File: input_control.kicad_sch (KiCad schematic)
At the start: 17 parts, among them SW400 100SP1T1B4M2QE, SW401 100SP1T1B4M2QE, U400 CD4051BM

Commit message: pcb setup
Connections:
- no-connect marks 0 -> 16
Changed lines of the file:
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@@
 		(color 0 0 0 0)
 	)
+	(no_connect
+		(at 217.17 93.98)
+	)
+	(no_connect
+		(at 161.29 93.98)
+	)
+	(no_connect
+		(at 161.29 96.52)
+	)
+	(no_connect
+		(at 189.23 93.98)
+	)
+	(no_connect
+		(at 189.23 46.99)
+	)
+	(no_connect
+		(at 161.29 46.99)
+	)
+	(no_connect
+		(at 245.11 93.98)
+	)
+	(no_connect
+		(at 217.17 46.99)
+	)
+	(no_connect
+		(at 217.17 44.45)
+	)
+	(no_connect
+		(at 217.17 96.52)
+	)
+	(no_connect
+		(at 245.11 96.52)
+	)
+	(no_connect
+		(at 245.11 44.45)
+	)
+	(no_connect
+		(at 245.11 46.99)
+	)
+	(no_connect
+		(at 189.23 96.52)
+	)
+	(no_connect
+		(at 189.23 44.45)
+	)
+	(no_connect
+		(at 161.29 44.45)
+	)
 	(wire
 		(pts
@@
 		(dnp no)
 		(property "Reference" "VR406"
-			(at 243.84 46.736 0)
+			(at 243.84 50.292 0)
 			(effects
 				(font
@@
 		(pin "2"
 		)
+		(pin "NC1"
+		)
+		(pin "NC2"
+		)
 		(instances
 			(project "GalernaDsp"
@@
 		(dnp no)
 		(property "Reference" "VR401"
-			(at 160.02 96.266 0)
+			(at 160.02 100.076 0)
 			(effects
 				(font
@@
 		(pin "2"
 		)
+		(pin "NC1"
+		)
+		(pin "NC2"
+		)
 		(instances
 			(project "GalernaDsp"
@@
 		(dnp no)
 		(property "Reference" "VR407"
-			(at 243.84 96.266 0)
+			(at 243.84 100.076 0)
 			(effects
 				(font
@@
 		(pin "2"
 		)
+		(pin "NC1"
+		)
+		(pin "NC2"
+		)
 		(instances
 			(project "GalernaDsp"
@@
 		(dnp no)
 		(property "Reference" "VR402"
-			(at 187.96 46.736 0)
+			(at 187.96 50.292 0)
 			(effects
 				(font
@@
 		(pin "2"
 		)
+		(pin "NC1"
+		)
+		(pin "NC2"
+		)
 		(instances
 			(project "GalernaDsp"
@@
 		(dnp no)
 		(property "Reference" "VR400"
-			(at 160.02 46.736 0)
+			(at 160.02 50.292 0)
 			(effects
 				(font
@@
 		(pin "2"
 		)
+		(pin "NC2"
+		)
+		(pin "NC1"
+		)
 		(instances
 			(project ""
@@
 		(dnp no)
 		(property "Reference" "VR403"
-			(at 187.96 96.266 0)
+			(at 187.96 100.076 0)
 			(effects
 				(font
@@
 		(pin "2"
 		)
+		(pin "NC2"
+		)
+		(pin "NC1"
+		)
 		(instances
 			(project "GalernaDsp"
@@
 		(dnp no)
 		(property "Reference" "VR404"
-			(at 215.9 46.736 0)
+			(at 215.9 50.292 0)
 			(effects
 				(font
@@
 		(pin "2"
 		)
+		(pin "NC2"
+		)
+		(pin "NC1"
+		)
 		(instances
 			(project "GalernaDsp"
@@
 		(dnp no)
 		(property "Reference" "VR405"
-			(at 215.9 96.266 0)
+			(at 215.9 100.076 0)
 			(effects
 				(font
@@
 		(pin "2"
 		)
+		(pin "NC2"
+		)
+		(pin "NC1"
+		)
 		(instances

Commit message: last update
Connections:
- net POT_0_CTL: now also U400.15 (2); no longer U400.13 (0)
- net POT_1_CTL: now also U400.13 (0); no longer U400.14 (1)
- net POT_2_CTL: now also U400.14 (1); no longer U400.15 (2)
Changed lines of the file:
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@@
 		)
 	)
-	(label "POT_1_CTL"
+	(label "POT_2_CTL"
 		(at 83.82 66.04 0)
 		(effects
@@
 		)
 	)
-	(label "POT_0_CTL"
+	(label "POT_1_CTL"
 		(at 83.82 60.96 0)
 		(effects
@@
 		)
 	)
-	(label "POT_2_CTL"
+	(label "POT_0_CTL"
 		(at 83.82 71.12 0)
 		(effects

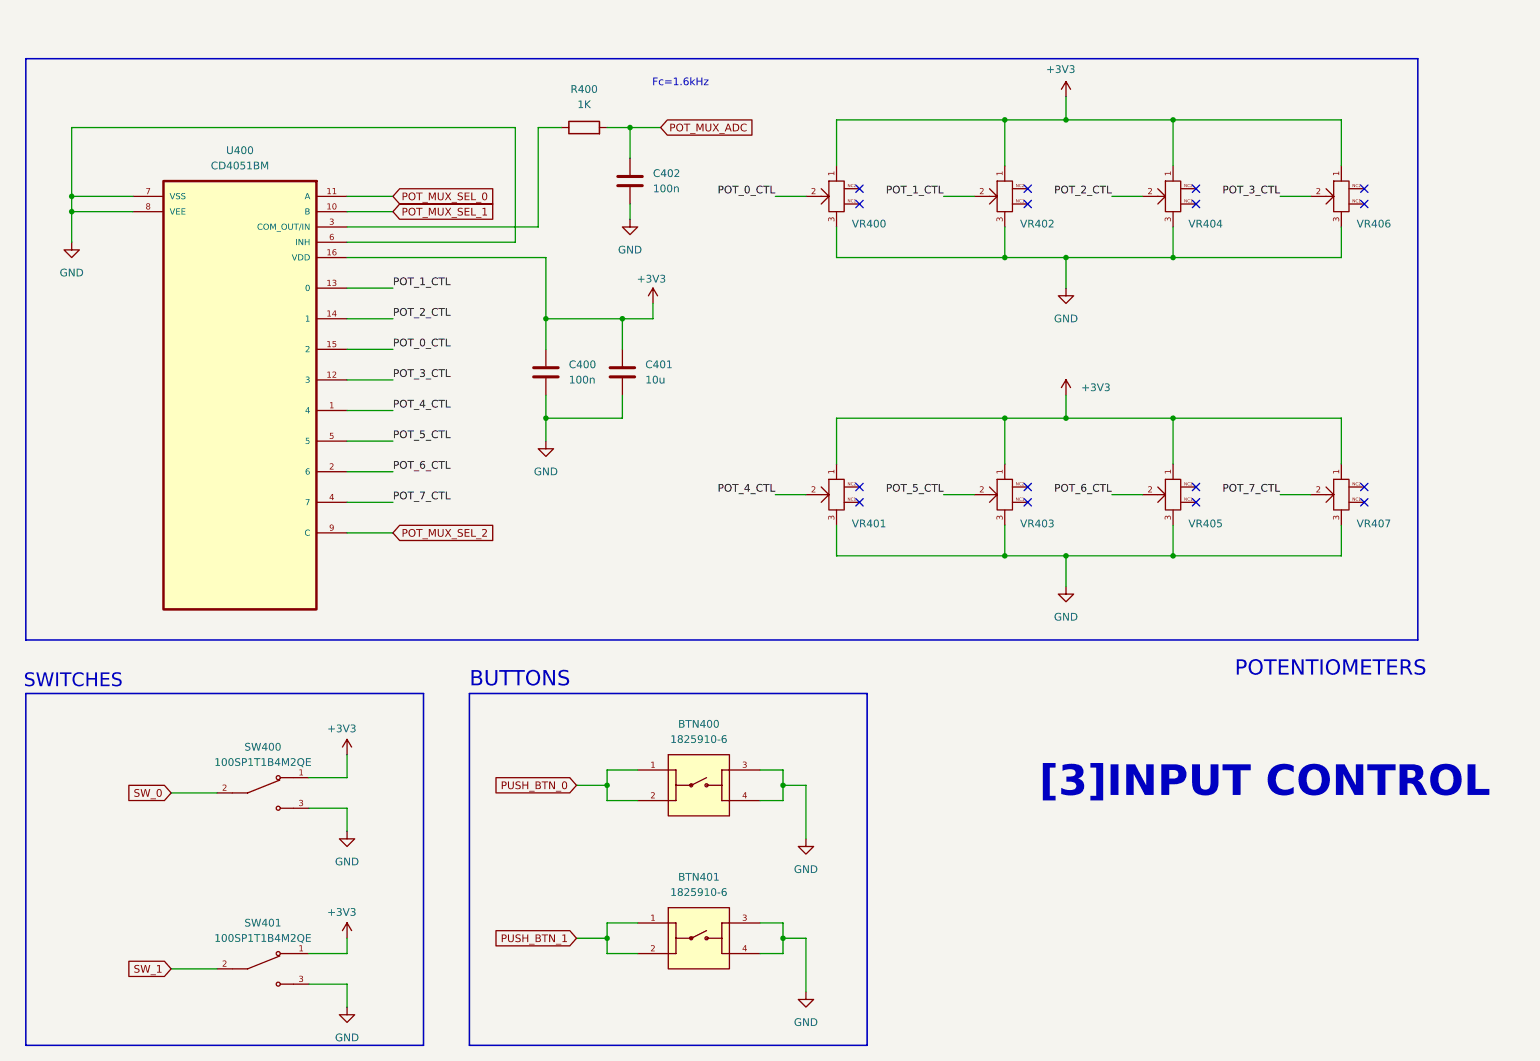
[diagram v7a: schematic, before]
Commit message: Codec updated to ES8388 on schematic
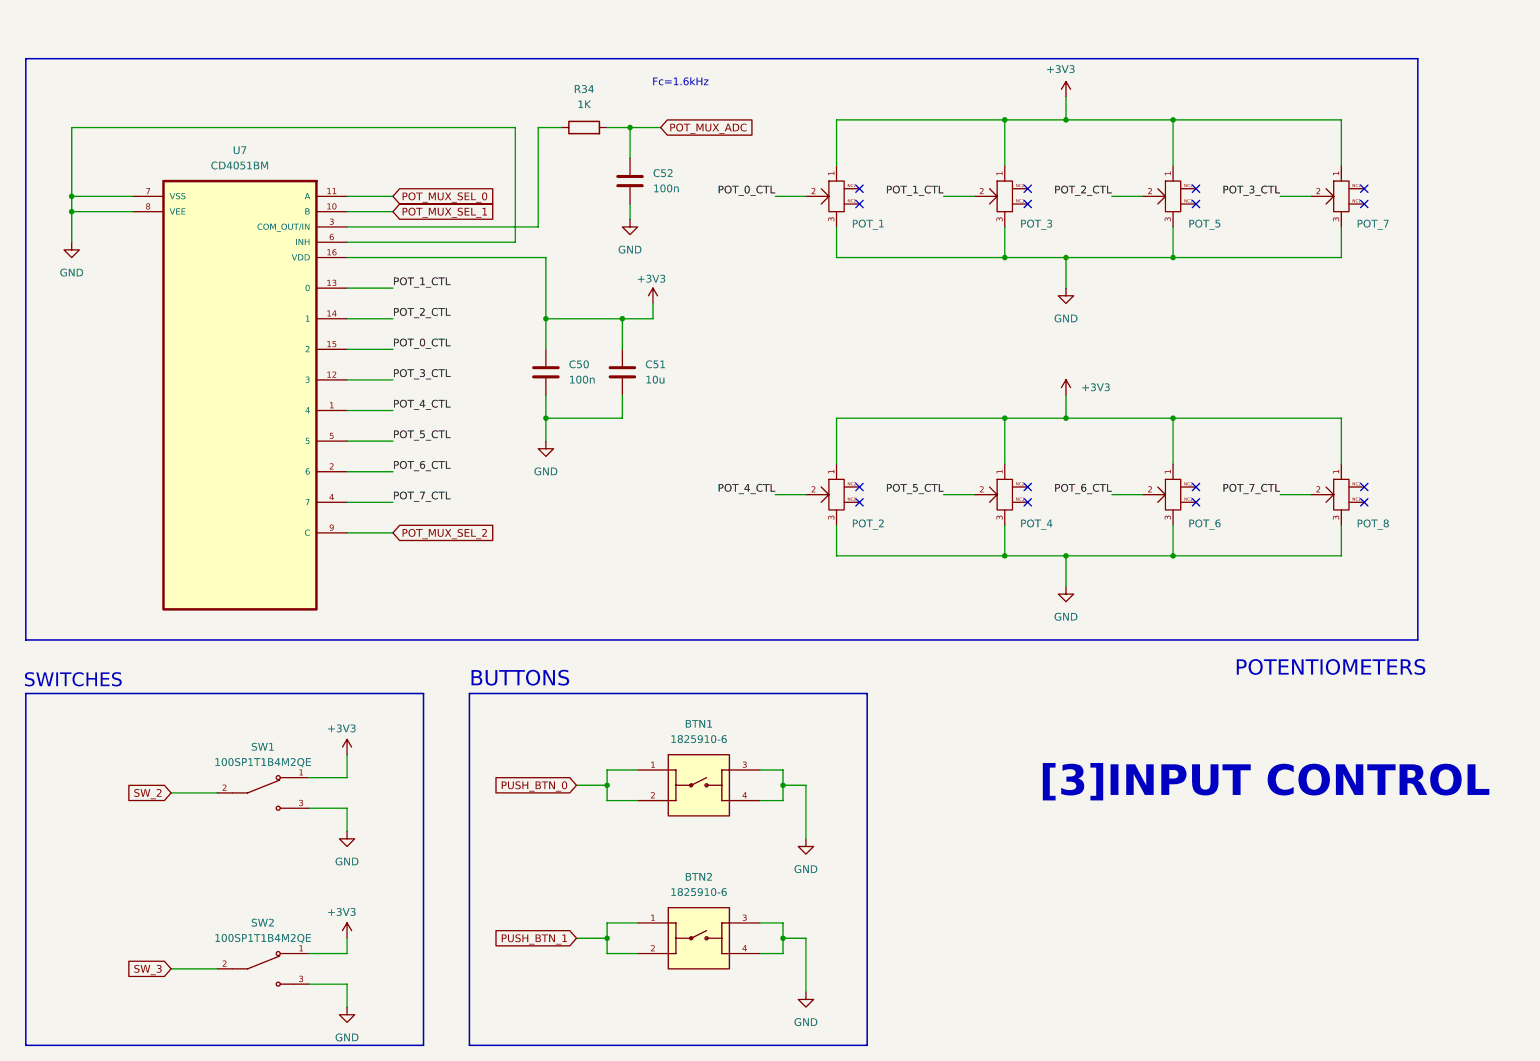
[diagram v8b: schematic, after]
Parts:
- renumbered BTN400 to BTN1, BTN401 to BTN2, C400 to C50, C401 to C51, C402 to C52, VR400 to POT_1, VR401 to POT_2, VR402 to POT_3, VR403 to POT_4, VR404 to POT_5, VR405 to POT_6, VR406 to POT_7, VR407 to POT_8, R400 to R34, SW400 to SW1, SW401 to SW2, U400 to U7
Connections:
- net SW_0 renamed SW_2
- net SW_1 renamed SW_3
